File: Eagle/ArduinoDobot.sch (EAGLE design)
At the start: 16 parts, among them X1 057-010-1

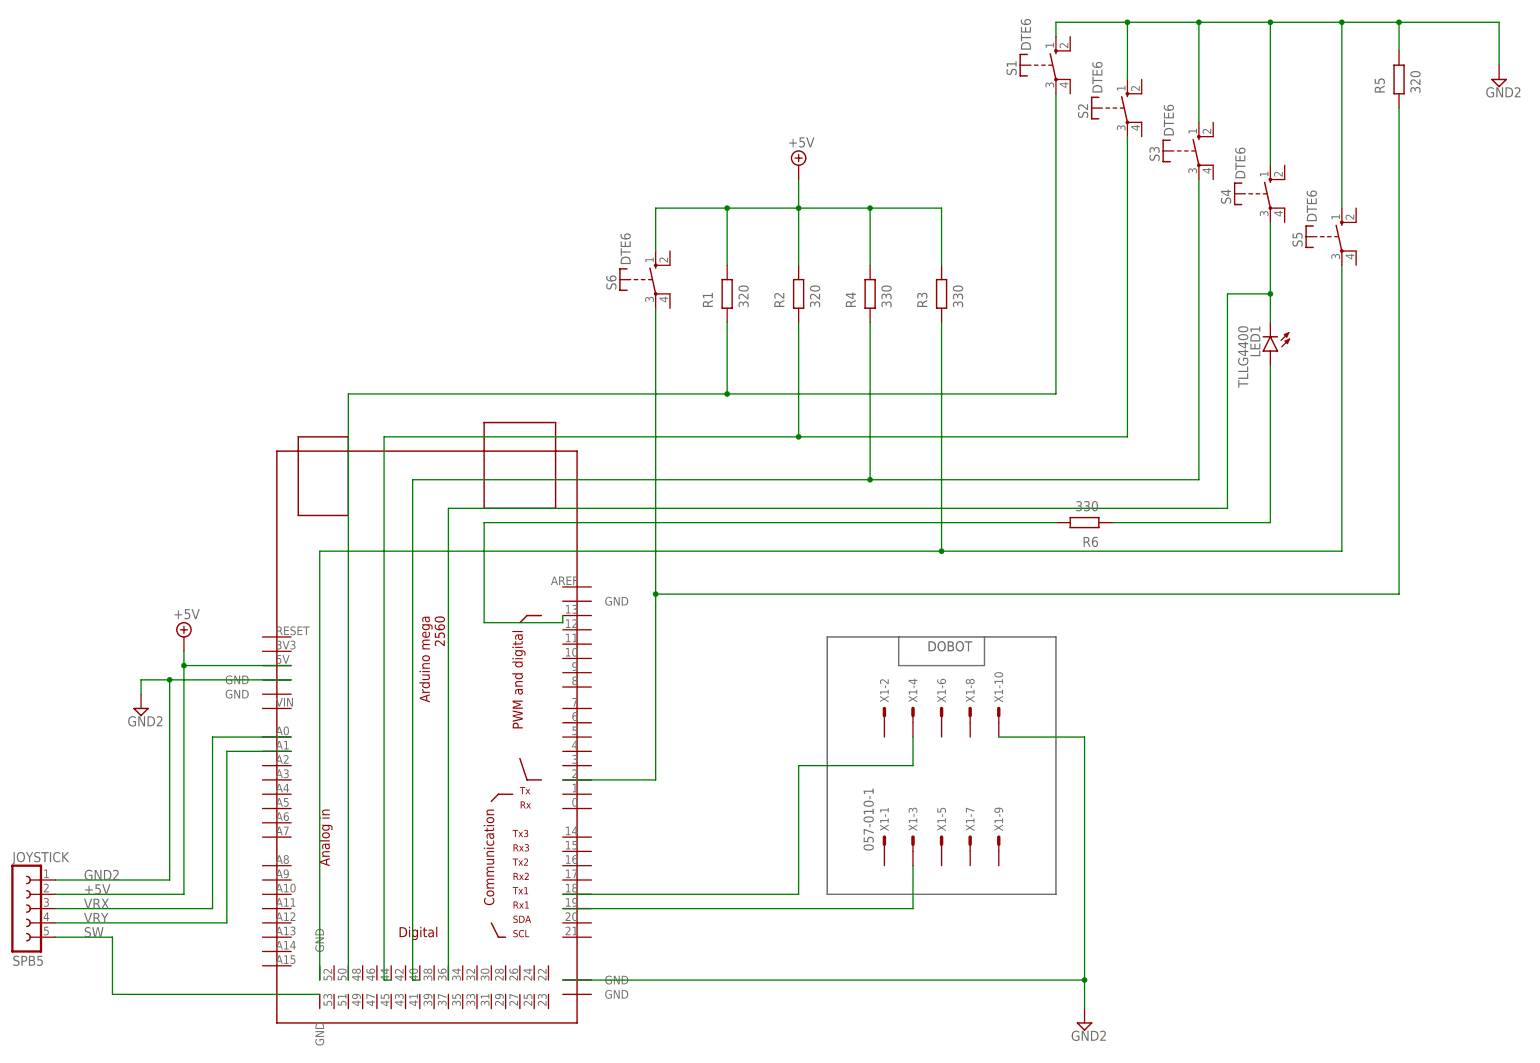
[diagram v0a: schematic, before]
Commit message: demo button added
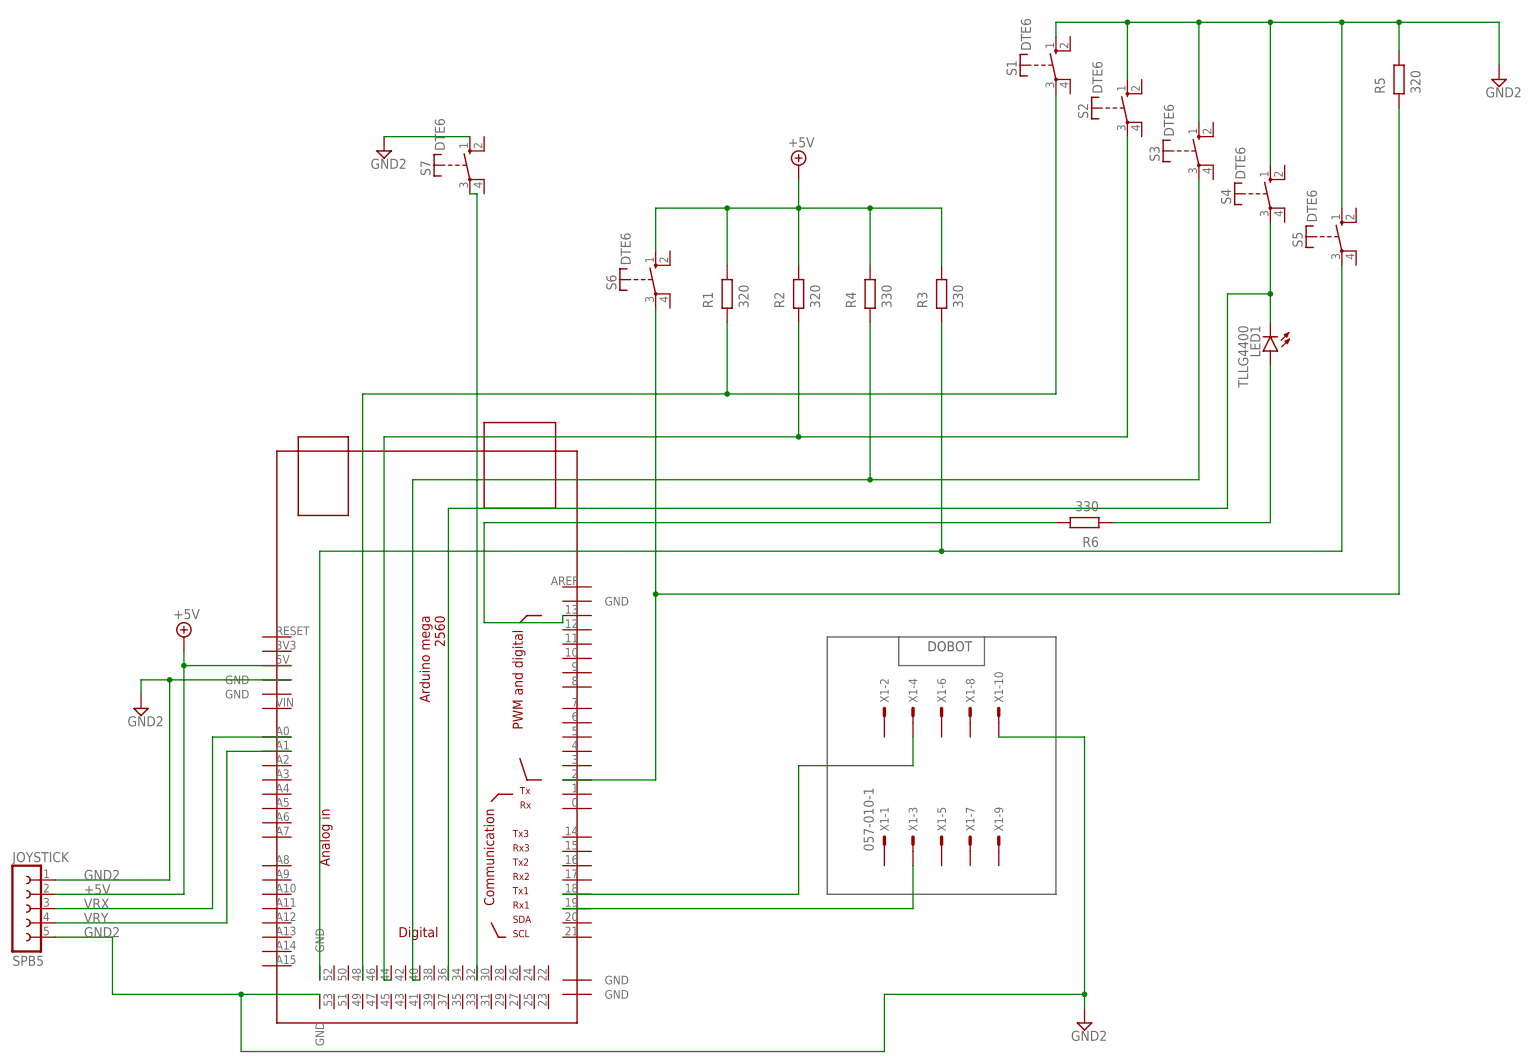
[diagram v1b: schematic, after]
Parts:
- added S7: DTE6, switch-misc:DTE6
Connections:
- removed net SW: JOYSTICK.5, U$1.GND@7
- new net N$2: S7.P, U$1.32
- net GND2: now also JOYSTICK.5, S7.S, U$1.GND@7; no longer U$1.GND@4
- net N$1: now also U$1.48; no longer U$1.50
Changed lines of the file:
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@@
 <part name="R6" library="ngspice-simulation" library_urn="urn:adsk.eagle:library:527439" deviceset="R" device="" value="330"/>
 <part name="SUPPLY5" library="supply2" library_urn="urn:adsk.eagle:library:372" deviceset="GND2" device=""/>
+<part name="SUPPLY6" library="supply2" library_urn="urn:adsk.eagle:library:372" deviceset="GND2" device=""/>
+<part name="S7" library="switch-misc" library_urn="urn:adsk.eagle:library:376" deviceset="DT" device="E6" package3d_urn="urn:adsk.eagle:package:27432/1"/>
 </parts>
 <sheets>
@@
 <instance part="SUPPLY5" gate="G$1" x="76.2" y="-50.8" smashed="yes">
 <attribute name="VALUE" x="73.787" y="-53.975" size="1.778" layer="96"/>
+</instance>
+<instance part="SUPPLY6" gate="G$1" x="-48.26" y="104.14" smashed="yes">
+<attribute name="VALUE" x="-50.673" y="100.965" size="1.778" layer="96"/>
+</instance>
+<instance part="S7" gate="1" x="-33.02" y="101.6" smashed="yes">
+<attribute name="NAME" x="-40.005" y="99.695" size="1.778" layer="95" rot="R90"/>
+<attribute name="VALUE" x="-37.465" y="104.14" size="1.778" layer="96" rot="R90"/>
 </instance>
 </instances>
@@
 <pinref part="X1" gate="-10" pin="S"/>
 <wire x1="60.96" y1="0" x2="76.2" y2="0" width="0.1524" layer="91"/>
-<wire x1="76.2" y1="0" x2="76.2" y2="-43.18" width="0.1524" layer="91"/>
-<pinref part="U$1" gate="G$1" pin="GND@4"/>
-<wire x1="76.2" y1="-43.18" x2="-16.51" y2="-43.18" width="0.1524" layer="91"/>
+<wire x1="76.2" y1="0" x2="76.2" y2="-45.72" width="0.1524" layer="91"/>
 <pinref part="SUPPLY5" gate="G$1" pin="GND2"/>
-<wire x1="76.2" y1="-48.26" x2="76.2" y2="-43.18" width="0.1524" layer="91"/>
-<junction x="76.2" y="-43.18"/>
+<wire x1="76.2" y1="-45.72" x2="76.2" y2="-48.26" width="0.1524" layer="91"/>
+<wire x1="76.2" y1="-45.72" x2="40.64" y2="-45.72" width="0.1524" layer="91"/>
+<wire x1="40.64" y1="-45.72" x2="40.64" y2="-55.88" width="0.1524" layer="91"/>
+<junction x="76.2" y="-45.72"/>
+<pinref part="U$1" gate="G$1" pin="GND@7"/>
+<wire x1="-59.69" y1="-45.72" x2="-73.66" y2="-45.72" width="0.1524" layer="91"/>
+<pinref part="JOYSTICK" gate="1" pin="5"/>
+<wire x1="-73.66" y1="-45.72" x2="-96.52" y2="-45.72" width="0.1524" layer="91"/>
+<wire x1="-96.52" y1="-45.72" x2="-96.52" y2="-35.56" width="0.1524" layer="91"/>
+<wire x1="-96.52" y1="-35.56" x2="-106.68" y2="-35.56" width="0.1524" layer="91"/>
+<label x="-101.6" y="-35.56" size="1.778" layer="95"/>
+<wire x1="40.64" y1="-55.88" x2="-73.66" y2="-55.88" width="0.1524" layer="91"/>
+<wire x1="-73.66" y1="-55.88" x2="-73.66" y2="-45.72" width="0.1524" layer="91"/>
+<junction x="-73.66" y="-45.72"/>
+</segment>
+<segment>
+<pinref part="SUPPLY6" gate="G$1" pin="GND2"/>
+<pinref part="S7" gate="1" pin="S"/>
+<wire x1="-48.26" y1="106.68" x2="-33.02" y2="106.68" width="0.1524" layer="91"/>
 </segment>
 </net>
 <net name="N$1" class="0">
 <segment>
-<pinref part="U$1" gate="G$1" pin="50"/>
-<wire x1="-54.61" y1="-43.18" x2="-54.61" y2="60.96" width="0.1524" layer="91"/>
-<wire x1="-54.61" y1="60.96" x2="12.7" y2="60.96" width="0.1524" layer="91"/>
 <pinref part="S1" gate="1" pin="P"/>
+<wire x1="-52.07" y1="60.96" x2="12.7" y2="60.96" width="0.1524" layer="91"/>
 <wire x1="12.7" y1="60.96" x2="71.12" y2="60.96" width="0.1524" layer="91"/>
 <wire x1="71.12" y1="114.3" x2="71.12" y2="60.96" width="0.1524" layer="91"/>
@@
 <wire x1="12.7" y1="73.66" x2="12.7" y2="60.96" width="0.1524" layer="91"/>
 <junction x="12.7" y="60.96"/>
+<pinref part="U$1" gate="G$1" pin="48"/>
+<wire x1="-52.07" y1="-43.18" x2="-52.07" y2="60.96" width="0.1524" layer="91"/>
 </segment>
 </net>
@@
 </segment>
 </net>
-<net name="SW" class="0">
-<segment>
-<pinref part="U$1" gate="G$1" pin="GND@7"/>
-<wire x1="-59.69" y1="-45.72" x2="-96.52" y2="-45.72" width="0.1524" layer="91"/>
-<pinref part="JOYSTICK" gate="1" pin="5"/>
-<wire x1="-96.52" y1="-45.72" x2="-96.52" y2="-35.56" width="0.1524" layer="91"/>
-<wire x1="-96.52" y1="-35.56" x2="-106.68" y2="-35.56" width="0.1524" layer="91"/>
-<label x="-101.6" y="-35.56" size="1.778" layer="95"/>
-</segment>
-</net>
 <net name="VRY" class="0">
 <segment>
@@
 </segment>
 </net>
+<net name="N$2" class="0">
+<segment>
+<pinref part="S7" gate="1" pin="P"/>
+<pinref part="U$1" gate="G$1" pin="32"/>
+<wire x1="-33.02" y1="96.52" x2="-31.75" y2="96.52" width="0.1524" layer="91"/>
+<wire x1="-31.75" y1="96.52" x2="-31.75" y2="-43.18" width="0.1524" layer="91"/>
+</segment>
+</net>
